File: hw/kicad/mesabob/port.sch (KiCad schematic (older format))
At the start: 5 parts, among them J1 RJ45, U1 rs4854

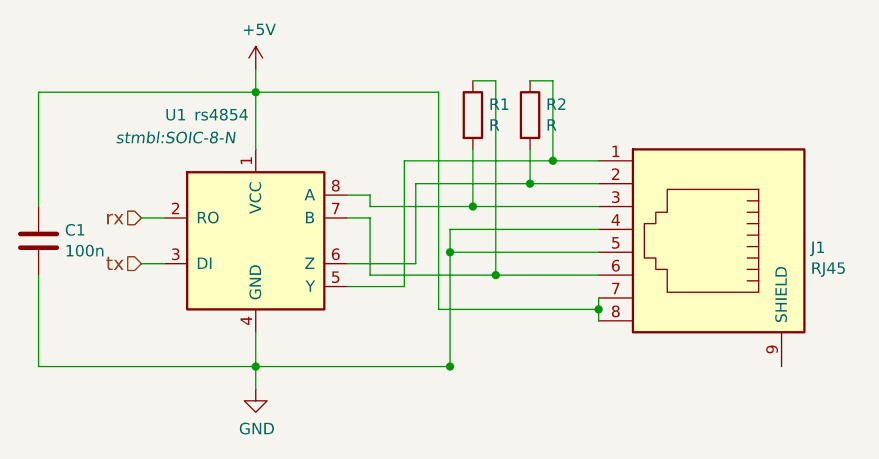
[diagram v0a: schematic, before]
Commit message: mesabob pinout fix
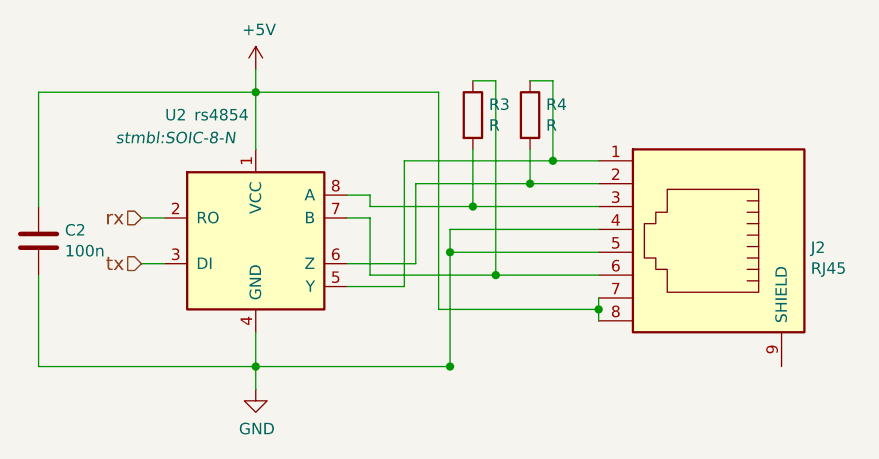
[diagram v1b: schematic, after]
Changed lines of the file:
@@
 LIBS:stmbl
 LIBS:mesabob-cache
-EELAYER 25 0
+EELAYER 26 0
 EELAYER END
 $Descr A4 11693 8268
 encoding utf-8
-Sheet 2 9
+Sheet 3 9
 Title ""
 Date ""
@@
 AR Path="/59239C3C/59238920" Ref="J7"  Part="1"
 AR Path="/59239C46/59238920" Ref="J8"  Part="1"
-F 0 "J1" V 7280 4028 50  0000 L CNN
+F 0 "J2" V 7280 4028 50  0000 L CNN
 F 1 "RJ45" V 7371 4028 50  0000 L CNN
 F 2 "Connect:RJ45_8" H 7250 3550 50  0001 C CNN
@@
 AR Path="/59239C3C/59238927" Ref="U7"  Part="1"
 AR Path="/59239C46/59238927" Ref="U8"  Part="1"
-F 0 "U1" H 4950 4100 50  0000 C CNN
+F 0 "U2" H 4950 4100 50  0000 C CNN
 F 1 "rs4854" H 5150 4100 50  0000 C CNN
 F 2 "stmbl:SOIC-8-N" H 4950 4000 50  0000 C CIN
@@
 AR Path="/59239C3C/5923892E" Ref="#PWR017"  Part="1"
 AR Path="/59239C46/5923892E" Ref="#PWR019"  Part="1"
-F 0 "#PWR05" H 5300 2650 50  0001 C CNN
+F 0 "#PWR07" H 5300 2650 50  0001 C CNN
 F 1 "+5V" H 5315 2973 50  0000 C CNN
 F 2 "" H 5300 2800 50  0000 C CNN
@@
 AR Path="/59239C3C/59238934" Ref="#PWR018"  Part="1"
 AR Path="/59239C46/59238934" Ref="#PWR020"  Part="1"
-F 0 "#PWR06" H 5300 3950 50  0001 C CNN
+F 0 "#PWR08" H 5300 3950 50  0001 C CNN
 F 1 "GND" H 5305 4027 50  0000 C CNN
 F 2 "" H 5300 4200 50  0000 C CNN
@@
 AR Path="/59239C3C/59238958" Ref="C7"  Part="1"
 AR Path="/59239C46/59238958" Ref="C8"  Part="1"
-F 0 "C1" H 4465 3596 50  0000 L CNN
+F 0 "C2" H 4465 3596 50  0000 L CNN
 F 1 "100n" H 4465 3505 50  0000 L CNN
 F 2 "stmbl:C_0603" H 4388 3400 50  0001 C CNN
@@
 AR Path="/59239C3C/5923C5AD" Ref="R13"  Part="1"
 AR Path="/59239C46/5923C5AD" Ref="R15"  Part="1"
-F 0 "R1" H 6320 3046 50  0000 L CNN
+F 0 "R3" H 6320 3046 50  0000 L CNN
 F 1 "R" H 6320 2955 50  0000 L CNN
 F 2 "stmbl:R_0603" V 6180 3000 50  0001 C CNN
@@
 AR Path="/59239C3C/5923C5FE" Ref="R14"  Part="1"
 AR Path="/59239C46/5923C5FE" Ref="R16"  Part="1"
-F 0 "R2" H 6570 3046 50  0000 L CNN
+F 0 "R4" H 6570 3046 50  0000 L CNN
 F 1 "R" H 6570 2955 50  0000 L CNN
 F 2 "stmbl:R_0603" V 6430 3000 50  0001 C CNN

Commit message: add polymer caps and make zone more nicer
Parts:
- C1: symbol C -> stmbl1:C
- J1: symbol RJ45 -> mesabob-rescue:RJ45
- R1, R2: symbol R -> stmbl1:R
- U1: symbol rs4854 -> stmbl1:rs4854
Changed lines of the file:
@@
-EESchema Schematic File Version 2
-LIBS:power
-LIBS:device
-LIBS:transistors
-LIBS:conn
-LIBS:linear
-LIBS:regul
-LIBS:74xx
-LIBS:cmos4000
-LIBS:adc-dac
-LIBS:memory
-LIBS:xilinx
-LIBS:microcontrollers
-LIBS:dsp
-LIBS:microchip
-LIBS:analog_switches
-LIBS:motorola
-LIBS:texas
-LIBS:intel
-LIBS:audio
-LIBS:interface
-LIBS:digital-audio
-LIBS:philips
-LIBS:display
-LIBS:cypress
-LIBS:siliconi
-LIBS:opto
-LIBS:atmel
-LIBS:contrib
-LIBS:valves
-LIBS:stmbl
+EESchema Schematic File Version 4
 LIBS:mesabob-cache
-EELAYER 26 0
+EELAYER 29 0
 EELAYER END
 $Descr A4 11693 8268
 encoding utf-8
-Sheet 3 9
+Sheet 2 9
 Title ""
 Date ""
@@
 $EndDescr
 $Comp
-L RJ45 J1
+L mesabob-rescue:RJ45 J1
 U 1 1 59238920
 P 7250 3550
@@
 AR Path="/59239C3C/59238920" Ref="J7"  Part="1"
 AR Path="/59239C46/59238920" Ref="J8"  Part="1"
-F 0 "J2" V 7280 4028 50  0000 L CNN
+F 0 "J1" V 7280 4028 50  0000 L CNN
 F 1 "RJ45" V 7371 4028 50  0000 L CNN
 F 2 "Connect:RJ45_8" H 7250 3550 50  0001 C CNN
@@
 $EndComp
 $Comp
-L rs4854 U1
+L stmbl1:rs4854 U1
 U 1 1 59238927
 P 5300 3550
@@
 AR Path="/59239C3C/59238927" Ref="U7"  Part="1"
 AR Path="/59239C46/59238927" Ref="U8"  Part="1"
-F 0 "U2" H 4950 4100 50  0000 C CNN
+F 0 "U1" H 4950 4100 50  0000 C CNN
 F 1 "rs4854" H 5150 4100 50  0000 C CNN
 F 2 "stmbl:SOIC-8-N" H 4950 4000 50  0000 C CIN
@@
 $EndComp
 $Comp
-L +5V #PWR05
+L power:+5V #PWR05
 U 1 1 5923892E
 P 5300 2800
@@
 AR Path="/59239C3C/5923892E" Ref="#PWR017"  Part="1"
 AR Path="/59239C46/5923892E" Ref="#PWR019"  Part="1"
-F 0 "#PWR07" H 5300 2650 50  0001 C CNN
+F 0 "#PWR05" H 5300 2650 50  0001 C CNN
 F 1 "+5V" H 5315 2973 50  0000 C CNN
 F 2 "" H 5300 2800 50  0000 C CNN
@@
 $EndComp
 $Comp
-L GND #PWR06
+L power:GND #PWR06
 U 1 1 59238934
 P 5300 4200
@@
 AR Path="/59239C3C/59238934" Ref="#PWR018"  Part="1"
 AR Path="/59239C46/59238934" Ref="#PWR020"  Part="1"
-F 0 "#PWR08" H 5300 3950 50  0001 C CNN
+F 0 "#PWR06" H 5300 3950 50  0001 C CNN
 F 1 "GND" H 5305 4027 50  0000 C CNN
 F 2 "" H 5300 4200 50  0000 C CNN
@@
 rx
 $Comp
-L C C1
+L stmbl1:C C1
 U 1 1 59238958
 P 4350 3550
@@
 AR Path="/59239C3C/59238958" Ref="C7"  Part="1"
 AR Path="/59239C46/59238958" Ref="C8"  Part="1"
-F 0 "C2" H 4465 3596 50  0000 L CNN
+F 0 "C1" H 4465 3596 50  0000 L CNN
 F 1 "100n" H 4465 3505 50  0000 L CNN
 F 2 "stmbl:C_0603" H 4388 3400 50  0001 C CNN
@@
 $EndComp
 $Comp
-L R R1
+L stmbl1:R R1
 U 1 1 5923C5AD
 P 6250 3000
@@
 AR Path="/59239C3C/5923C5AD" Ref="R13"  Part="1"
 AR Path="/59239C46/5923C5AD" Ref="R15"  Part="1"
-F 0 "R3" H 6320 3046 50  0000 L CNN
+F 0 "R1" H 6320 3046 50  0000 L CNN
 F 1 "R" H 6320 2955 50  0000 L CNN
 F 2 "stmbl:R_0603" V 6180 3000 50  0001 C CNN
@@
 $EndComp
 $Comp
-L R R2
+L stmbl1:R R2
 U 1 1 5923C5FE
 P 6500 3000
@@
 AR Path="/59239C3C/5923C5FE" Ref="R14"  Part="1"
 AR Path="/59239C46/5923C5FE" Ref="R16"  Part="1"
-F 0 "R4" H 6570 3046 50  0000 L CNN
+F 0 "R2" H 6570 3046 50  0000 L CNN
 F 1 "R" H 6570 2955 50  0000 L CNN
 F 2 "stmbl:R_0603" V 6430 3000 50  0001 C CNN
@@
 $EndComp
 Wire Wire Line
-	5300 2800 5300 3150
-Wire Wire Line
-	5300 3950 5300 4200
+	5300 2800 5300 2900
+Wire Wire Line
+	5300 3950 5300 4100
 Wire Wire Line
 	5700 3750 5950 3750
@@
 	5950 3750 5950 3200
 Wire Wire Line
-	5950 3200 6800 3200
+	5950 3200 6600 3200
 Wire Wire Line
 	5700 3650 6000 3650
@@
 	6000 3650 6000 3300
 Wire Wire Line
-	6000 3300 6800 3300
-Wire Wire Line
-	5800 3400 6800 3400
+	6000 3300 6500 3300
+Wire Wire Line
+	5800 3400 6250 3400
 Wire Wire Line
 	5800 3400 5800 3350
@@
 	5800 3450 5800 3700
 Wire Wire Line
-	5800 3700 6800 3700
+	5800 3700 6350 3700
 Wire Wire Line
 	6800 3500 6150 3500
 Wire Wire Line
-	6150 3500 6150 4100
+	6150 3500 6150 3600
 Wire Wire Line
 	6150 3600 6800 3600
@@
 Connection ~ 5300 4100
 Wire Wire Line
-	6800 3800 6800 3900
-Wire Wire Line
-	4350 2900 6100 2900
+	6800 3800 6800 3850
+Wire Wire Line
+	4350 2900 5300 2900
 Connection ~ 5300 2900
 Wire Wire Line
@@
 	6100 3850 6100 2900
 Connection ~ 6800 3850
-Connection ~ 6150 4100
 Wire Wire Line
 	4800 3450 4900 3450
@@
 	4350 4100 4350 3700
 Wire Wire Line
-	6150 4100 4350 4100
-Wire Wire Line
-	6250 3150 6250 3150
+	6150 4100 5300 4100
 Wire Wire Line
 	6250 3150 6250 3400
@@
 	6600 2850 6600 3200
 Connection ~ 6600 3200
+Wire Wire Line
+	6150 3600 6150 4100
+Wire Wire Line
+	5300 4100 5300 4200
+Wire Wire Line
+	5300 4100 4350 4100
+Wire Wire Line
+	5300 2900 5300 3150
+Wire Wire Line
+	5300 2900 6100 2900
+Wire Wire Line
+	6800 3850 6800 3900
+Wire Wire Line
+	6250 3400 6800 3400
+Wire Wire Line
+	6350 3700 6800 3700
+Wire Wire Line
+	6500 3300 6800 3300
+Wire Wire Line
+	6600 3200 6800 3200
 $EndSCHEMATC
